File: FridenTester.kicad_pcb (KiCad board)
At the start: 4 copper layers, 18.5 x 40.4 mm, 22 parts, among them P1 CONN_02X05, U1 BSD223P, U10 BSD223P, U11 BSD223P, U12 2N7002DN, U13 2N7002DN, U14 BSD223P, U15 BSD223P, U16 2N7002DN, U17 2N7002DN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

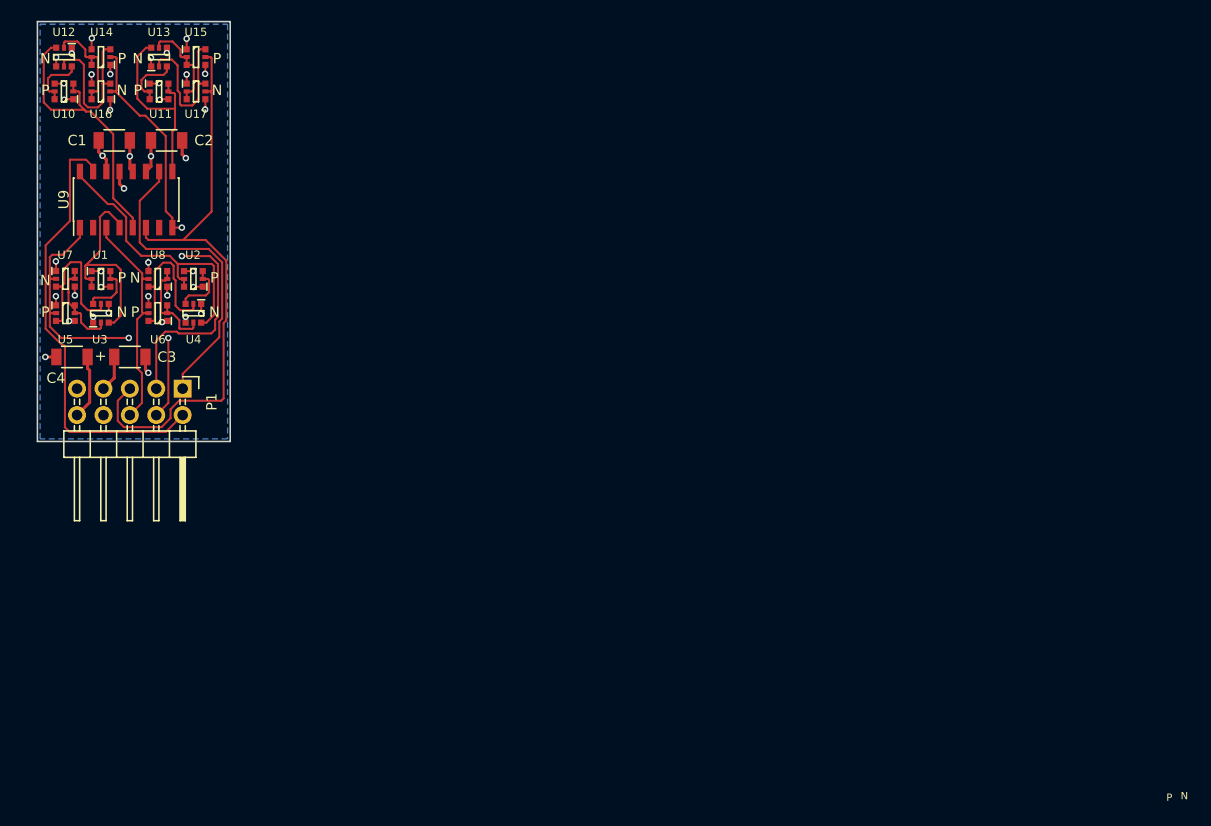
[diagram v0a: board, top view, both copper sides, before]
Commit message: Revision C, with gate drivers instead of mosfets
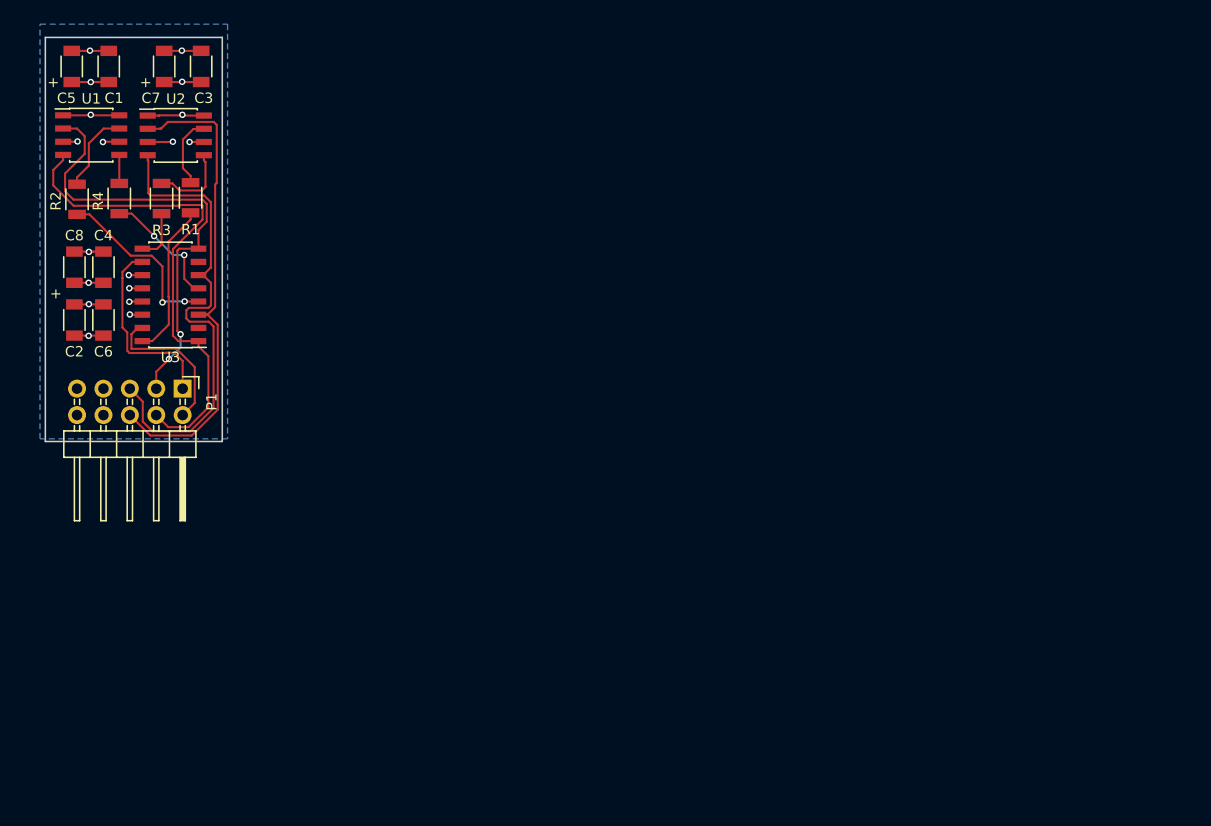
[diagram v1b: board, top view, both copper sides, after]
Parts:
- removed U10, U11, U14, U15, U5, U6: BSD223P, friden-footprints:SOT-363
- removed U12, U13, U16, U17, U4, U7, U8: 2N7002DN, friden-footprints:SOT-363
- removed U9: DG403, Housings_SOIC:SOIC-16_3.9x9.9mm_Pitch1.27mm
- added C5: 1u, Capacitors_SMD:C_1206, F.Cu at (35.3, 27.2)
- added C6: 1u, Capacitors_SMD:C_1206, F.Cu at (38.4, 51.6)
- added C7: 1u, Capacitors_SMD:C_1206, F.Cu at (44.2, 27.2)
- added C8: 1u, Capacitors_SMD:C_1206, F.Cu at (35.6, 46.5)
- added R1: 120, Resistors_SMD:R_1206, F.Cu at (46.7, 39.8)
- added R2: 50, Resistors_SMD:R_1206, F.Cu at (35.8, 40.0)
- added R3: 120, Resistors_SMD:R_1206, F.Cu at (43.9, 39.9)
- added R4: 50, Resistors_SMD:R_1206, F.Cu at (39.9, 39.9)
- C3, C4: value 1u -> 100n
- U1, U2: value BSD223P -> 2EDN752; footprint friden-footprints:SOT-363 -> Housings_SOIC:SOIC-8_3.9x4.9mm_Pitch1.27mm
- U3: value 2N7002DN -> DG403; footprint friden-footprints:SOT-363 -> Housings_SOIC:SOIC-16_3.9x9.9mm_Pitch1.27mm
- moved C3 28.8 mm to (47.8, 27.2), turned to 90 degrees
- moved C2 19.4 mm to (35.6, 51.6), turned to 270 degrees
- moved U2 13.9 mm to (45.3, 33.8), turned to 0 degrees
- moved U1 13.9 mm to (37.2, 33.8)
- moved C4 9.15 mm to (38.4, 46.5), turned to 90 degrees
- moved C1 7.13 mm to (38.9, 27.2), turned to 90 degrees
- moved U3 6.91 mm to (44.8, 49.1), turned to 180 degrees
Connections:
- C2 pad 1: +12V -> VDD
- C3 pad 1: VDD -> +12V
- U1 pad 2: /OUT5A -> /IO12B
- U1 pad 3: /OUT5A -> GNDREF
- U1 pad 4: VDD -> /IO12A
- U1 pad 5: /-OUT5A -> /OUT5B
- U1 pad 6: /-OUT5A -> VDD
- U2 pad 2: /-OUT12A -> /IO5A
- U2 pad 3: /-OUT12A -> GNDREF
- U2 pad 4: +12V -> /IO5B
- U2 pad 5: /OUT12A -> /OUT12B
- U2 pad 6: /OUT12A -> +12V
- U3 pad 1: GNDREF -> /IO12A
- U3 pad 2: /-IN12A -> (no net)
- U3 pad 3: /OUT5A -> /IO5A
- U3 pad 4: GNDREF -> Net-(R2-Pad2)
- U3 pad 5: /IN12A_BUF -> Net-(R4-Pad1)
- U3 pad 6: /-OUT5A -> /IO5B
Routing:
- net /SW_A: track 42.7 -> 14.6 mm
- net /IO5A: track 21.5 -> 46.8 mm
- net /OUT5B: track 27.3 -> 2.74 mm
- net /OUT12A: track 27.2 -> 6.88 mm
- net Net-(R2-Pad2): track 0.00 -> 17.3 mm, vias 0 -> 2
- net /IO12A: track 32.2 -> 48.0 mm, vias 2 -> 0
- net /IN12B_BUF: track 15.0 -> 0.00 mm
- net Net-(R1-Pad2): track 0.00 -> 14.8 mm
- net /IN12A_BUF: track 14.8 -> 0.00 mm
- net /IN5B_BUF: track 14.6 -> 0.00 mm
- net /IN5A_BUF: track 14.6 -> 0.00 mm
- net /OUT5A: track 20.5 -> 7.92 mm
- net Net-(R4-Pad1): track 0.00 -> 11.9 mm, vias 0 -> 2
- net /IO5B: track 58.5 -> 47.0 mm
- net /OUT12B: track 19.0 -> 7.76 mm
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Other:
- board size 18.5 x 40.4 mm -> 17 x 38.9 mm
- board text added: "REV C 2 NOV 2016"
- board text removed: "N"
- board text removed: "P"
- board text removed: "REV B 28 OCT 2016"

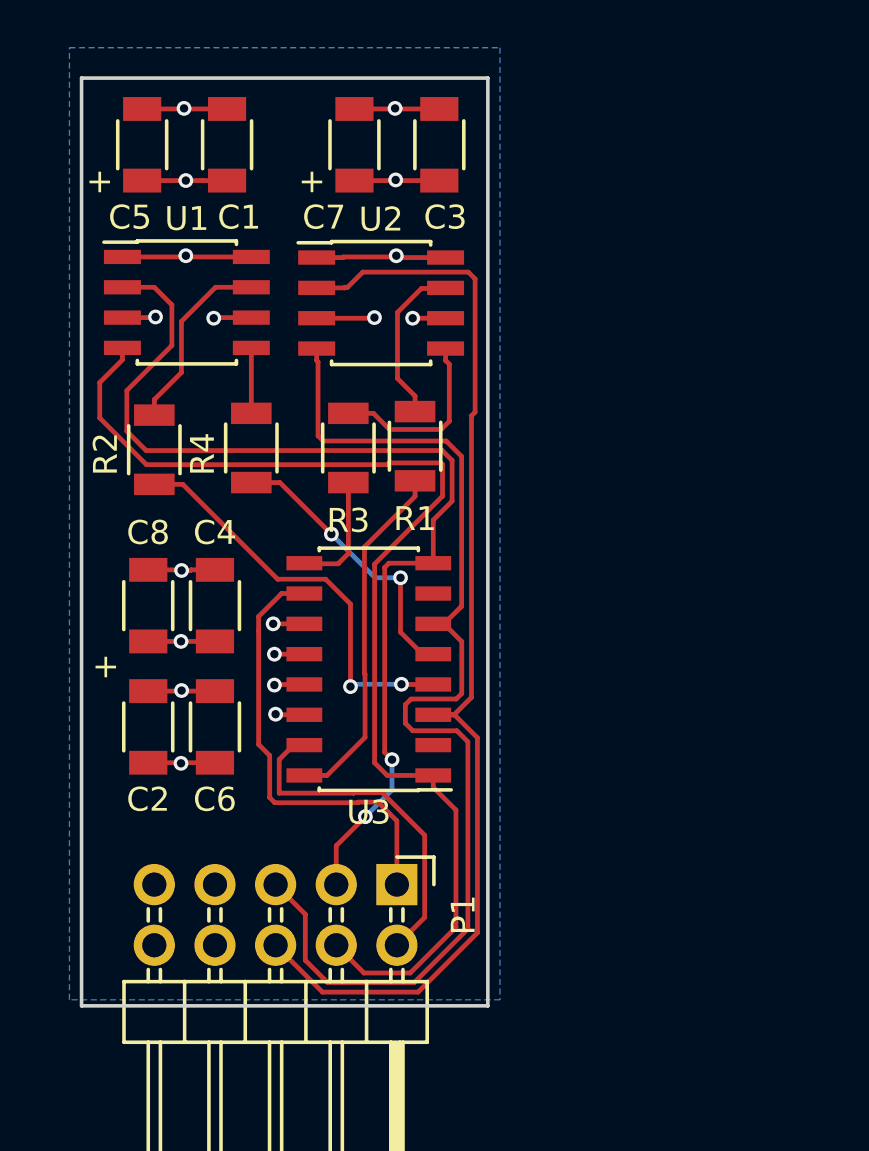
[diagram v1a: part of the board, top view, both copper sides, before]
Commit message: Start on rev D, with protection Schottkys
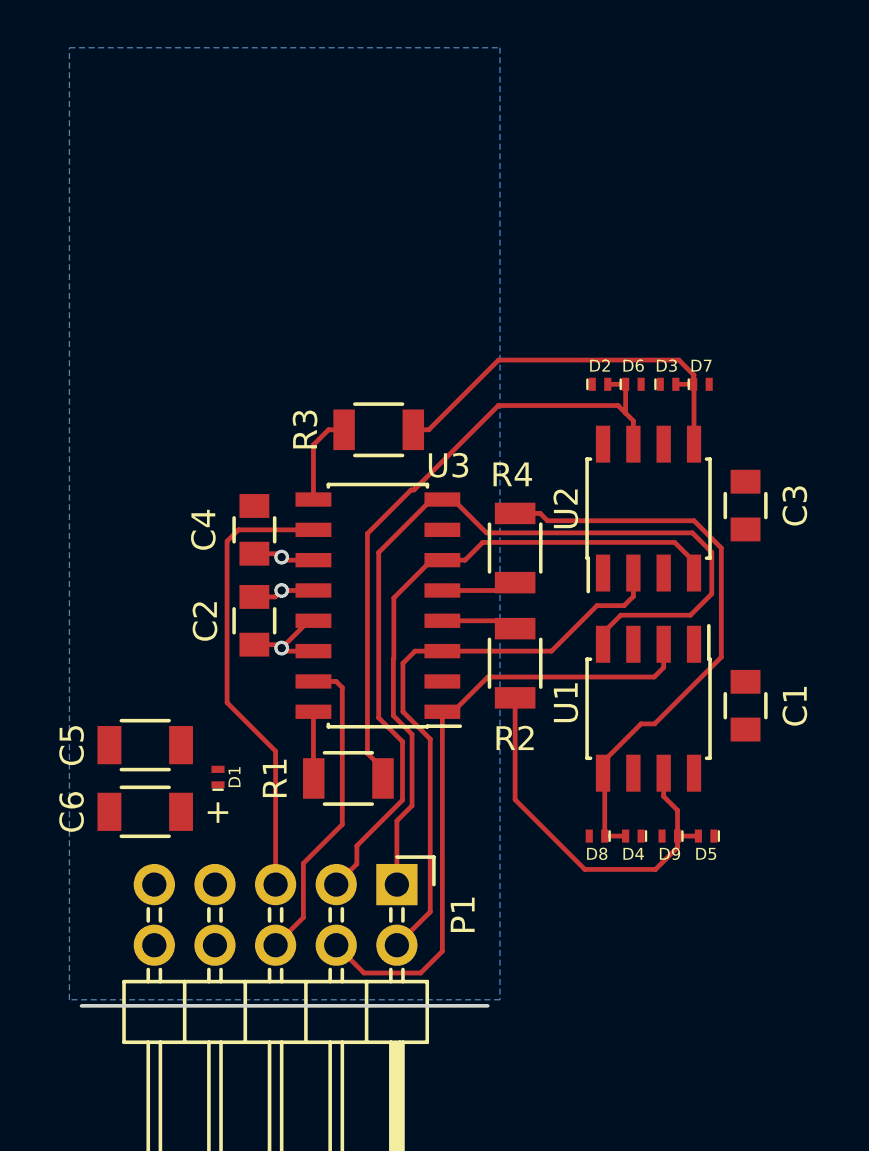
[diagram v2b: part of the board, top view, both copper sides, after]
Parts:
- removed C7, C8: 1u, Capacitors_SMD:C_1206
- added D1: CFSH05, friden-footprints:SOD-882L, F.Cu at (38.5, 53.7)
- added D2: CFSH05, friden-footprints:SOD-882L, F.Cu at (54.5, 37.2)
- added D3: CFSH05, friden-footprints:SOD-882L, F.Cu at (57.3, 37.2)
- added D4: CFSH05, friden-footprints:SOD-882L, F.Cu at (55.9, 56.1)
- added D5: CFSH05, friden-footprints:SOD-882L, F.Cu at (58.9, 56.1)
- added D6: CFSH05, friden-footprints:SOD-882L, F.Cu at (55.9, 37.2)
- added D7: CFSH05, friden-footprints:SOD-882L, F.Cu at (58.7, 37.2)
- added D8: CFSH05, friden-footprints:SOD-882L, F.Cu at (54.4, 56.1)
- added D9: CFSH05, friden-footprints:SOD-882L, F.Cu at (57.4, 56.1)
- C1, C2, C3, C4: footprint Capacitors_SMD:C_1206 -> Capacitors_SMD:C_0805
- moved C1 32.0 mm to (60.6, 50.7), turned to 270 degrees
- moved U1 25.8 mm to (56.5, 50.8), turned to 270 degrees
- moved C5 25.1 mm to (35.4, 52.3), turned to 180 degrees
- moved C3 19.8 mm to (60.6, 42.3), turned to 270 degrees
- moved R2 17.6 mm to (50.9, 48.9), turned to 90 degrees
- moved R1 14.2 mm to (43.9, 53.7), turned to 180 degrees
- moved U2 14.1 mm to (56.5, 42.4), turned to 90 degrees
- moved R4 11.8 mm to (50.9, 44.1)
- moved C2 6.29 mm to (40.0, 47.1)
- moved C6 4.60 mm to (35.4, 55.1), turned to 180 degrees
- moved C4 3.58 mm to (40.0, 43.3)
- moved U3 2.69 mm to (45.2, 46.5)
- moved R3 1.48 mm to (45.2, 39.1), turned to 0 degrees
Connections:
- C6 pad 1: VDD -> +12V
- P1 pad 1: /SW_B -> /IO5B
- P1 pad 10: +12V -> GNDREF
- P1 pad 2: /SW_A -> /IO5A
- P1 pad 5: /IO5B -> /SW_B
- P1 pad 6: /IO5A -> /SW_A
- P1 pad 8: GNDREF -> +12V
- U1 pad 2: /IO12B -> /IO12A
- U1 pad 4: /IO12A -> /IO12B
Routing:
- net /IO5A: track 46.8 -> 24.7 mm
- net /OUT5B: track 2.74 -> 24.6 mm
- net /IO12A: track 48.0 -> 26.3 mm
- net /OUT12A: track 6.88 -> 27.1 mm
- net /IO5B: track 47.0 -> 26.9 mm
- net GNDREF: track 19.1 -> 4.39 mm, vias 8 -> 1
- net Net-(R2-Pad2): track 17.3 -> 3.18 mm, vias 2 -> 0
- net VDD: track 14.7 -> 2.59 mm, vias 5 -> 1
- net Net-(R1-Pad2): track 14.8 -> 2.80 mm
- net +12V: track 14.5 -> 2.59 mm, vias 5 -> 1
- net /OUT12B: track 7.76 -> 16.9 mm
- net /OUT5A: track 7.92 -> 16.9 mm
- net Net-(R4-Pad1): track 11.9 -> 3.18 mm, vias 2 -> 0
- net /IO12B: track 43.7 -> 38.7 mm, vias 2 -> 0
- net /SW_A: track 14.6 -> 13.3 mm
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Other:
- board outline removed

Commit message: Revision D board layout
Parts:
- moved C3 9.40 mm to (51.6, 39.6), turned to 180 degrees
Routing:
- net VDD: track 2.59 -> 16.5 mm, vias 1 -> 8
- net GNDREF: track 4.39 -> 16.7 mm, vias 1 -> 11
- net +12V: track 2.59 -> 12.1 mm, vias 1 -> 6
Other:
- board outline added: 31.7 x 28.6 mm
- board text added: "2EDN7524"
- board text added: "C1-4 100n C5, C6 1u"
- board text added: "DG403"
- board text added: "R1 120R R2 50R R3 120R R4 50R"
- board text added: "REV D 19 NOV 2016"
- board text removed: "REV C 2 NOV 2016"
